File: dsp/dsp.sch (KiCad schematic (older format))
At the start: 29 parts

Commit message: Added ESP01 to DSPbox
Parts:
- added C? (x2): C, symbol C
- added U?: ESP01, symbol ESP01
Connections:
- net labels added: ESP_RX, ESP_TX
- wire segments 46 -> 51
- no-connect marks 13 -> 15
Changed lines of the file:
@@
 LIBS:valves
 LIBS:stm32f405rxtx
+LIBS:esp01
+LIBS:dsp-cache
 EELAYER 25 0
 EELAYER END
@@
 Text Label 7900 4600 0    60   ~ 0
 LCD_SCK
+$Comp
+L ESP01 U?
+U 1 1 574498BF
+P 5125 7250
+F 0 "U?" V 5175 7250 60  0000 C CNN
+F 1 "ESP01" V 5075 7250 60  0000 C CNN
+F 2 "" H 5125 7250 60  0000 C CNN
+F 3 "" H 5125 7250 60  0000 C CNN
+	1    5125 7250
+	1    0    0    -1
+$EndComp
+NoConn ~ 4525 7200
+NoConn ~ 4525 7300
+Wire Wire Line
+	5800 7300 5725 7300
+Wire Wire Line
+	5800 7000 5800 7300
+Wire Wire Line
+	5800 7200 5725 7200
+Wire Wire Line
+	5800 7100 5725 7100
+Connection ~ 5800 7200
+$Comp
+L +3V3 #PWR?
+U 1 1 57449FD5
+P 5800 7000
+F 0 "#PWR?" H 5800 6850 50  0001 C CNN
+F 1 "+3V3" H 5800 7140 50  0000 C CNN
+F 2 "" H 5800 7000 50  0000 C CNN
+F 3 "" H 5800 7000 50  0000 C CNN
+	1    5800 7000
+	1    0    0    -1
+$EndComp
+Connection ~ 5800 7100
+$Comp
+L C C?
+U 1 1 5744A312
+P 6375 7175
+F 0 "C?" H 6400 7275 50  0000 L CNN
+F 1 "C" H 6400 7075 50  0000 L CNN
+F 2 "" H 6413 7025 50  0000 C CNN
+F 3 "" H 6375 7175 50  0000 C CNN
+	1    6375 7175
+	1    0    0    -1
+$EndComp
+Wire Wire Line
+	5800 7025 6575 7025
+Connection ~ 5800 7025
+$Comp
+L C C?
+U 1 1 5744A47B
+P 6575 7175
+F 0 "C?" H 6600 7275 50  0000 L CNN
+F 1 "C" H 6600 7075 50  0000 L CNN
+F 2 "" H 6613 7025 50  0000 C CNN
+F 3 "" H 6575 7175 50  0000 C CNN
+	1    6575 7175
+	1    0    0    -1
+$EndComp
+Connection ~ 6375 7025
+$Comp
+L GND #PWR?
+U 1 1 5744A574
+P 6375 7325
+F 0 "#PWR?" H 6375 7075 50  0001 C CNN
+F 1 "GND" H 6375 7175 50  0000 C CNN
+F 2 "" H 6375 7325 50  0000 C CNN
+F 3 "" H 6375 7325 50  0000 C CNN
+	1    6375 7325
+	1    0    0    -1
+$EndComp
+$Comp
+L GND #PWR?
+U 1 1 5744A5C8
+P 6575 7325
+F 0 "#PWR?" H 6575 7075 50  0001 C CNN
+F 1 "GND" H 6575 7175 50  0000 C CNN
+F 2 "" H 6575 7325 50  0000 C CNN
+F 3 "" H 6575 7325 50  0000 C CNN
+	1    6575 7325
+	1    0    0    -1
+$EndComp
+Text Label 5725 7400 0    60   ~ 0
+ESP_TX
+Text Label 4525 7100 2    60   ~ 0
+ESP_RX
+$Comp
+L GND #PWR?
+U 1 1 5744B7D7
+P 4525 7400
+F 0 "#PWR?" H 4525 7150 50  0001 C CNN
+F 1 "GND" H 4525 7250 50  0000 C CNN
+F 2 "" H 4525 7400 50  0000 C CNN
+F 3 "" H 4525 7400 50  0000 C CNN
+	1    4525 7400
+	1    0    0    -1
+$EndComp
+Wire Notes Line
+	4175 6800 6750 6800
+Wire Notes Line
+	4175 6800 4175 7600
+Wire Notes Line
+	4175 7600 6750 7600
+Wire Notes Line
+	6750 7600 6750 6800
+Text Label 7900 4800 0    60   ~ 0
+ESP_RX
+Text Label 7900 4900 0    60   ~ 0
+ESP_TX
 $EndSCHEMATC

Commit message: Higher impedance inst inputs
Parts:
- removed C?: CP, symbol CP
- removed U? (x2): MCP601, symbol MCP601
- added C?: 100n, symbol C
- added U?: NE5532, symbol NE5532
- R?: value 1M -> 10M
- R?: value 100k -> 10M
- R?: value 10k -> 1M
- R?: value 100k -> 1M
- R? (x2): value 100R -> 100k
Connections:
- wire segments 51 -> 68
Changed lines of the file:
@@
 P 1900 1700
 F 0 "R?" H 1970 1746 50  0000 L CNN
-F 1 "1M" H 1970 1654 50  0000 L CNN
+F 1 "10M" H 1970 1654 50  0000 L CNN
 F 2 "" V 1830 1700 50  0000 C CNN
 F 3 "" H 1900 1700 50  0000 C CNN
@@
 $EndComp
 Wire Wire Line
-	1650 1550 2150 1550
+	1650 1550 1900 1550
+Wire Wire Line
+	1900 1550 2150 1550
 $Comp
 L GND #PWR?
@@
 P 2600 1350
 F 0 "R?" H 2670 1396 50  0000 L CNN
-F 1 "100k" H 2670 1304 50  0000 L CNN
+F 1 "10M" H 2670 1304 50  0000 L CNN
 F 2 "" V 2530 1350 50  0000 C CNN
 F 3 "" H 2600 1350 50  0000 C CNN
@@
 Wire Wire Line
 	2600 1550 2600 1500
-$Comp
-L MCP601 U?
-U 1 1 5743A901
-P 3600 1450
-F 0 "U?" H 3941 1496 50  0000 L CNN
-F 1 "MCP601" H 3941 1404 50  0000 L CNN
-F 2 "" H 3550 1550 50  0000 C CNN
-F 3 "" H 3650 1650 50  0000 C CNN
-	1    3600 1450
-	1    0    0    -1
-$EndComp
 Text Label 3300 1350 2    60   ~ 0
 VREF
@@
 P 3000 1550
 F 0 "R?" V 3208 1550 50  0000 C CNN
-F 1 "10k" V 3116 1550 50  0000 C CNN
+F 1 "1M" V 3116 1550 50  0000 C CNN
 F 2 "" V 2930 1550 50  0000 C CNN
 F 3 "" H 3000 1550 50  0000 C CNN
@@
 $EndComp
 Wire Wire Line
-	2450 1550 2850 1550
-Wire Wire Line
-	3150 1550 3300 1550
+	2450 1550 2600 1550
+Wire Wire Line
+	2600 1550 2850 1550
+Wire Wire Line
+	3150 1550 3200 1550
+Wire Wire Line
+	3200 1550 3300 1550
 $Comp
 L R R?
@@
 P 3700 2100
 F 0 "R?" V 3492 2100 50  0000 C CNN
-F 1 "100k" V 3584 2100 50  0000 C CNN
+F 1 "1M" V 3584 2100 50  0000 C CNN
 F 2 "" V 3630 2100 50  0000 C CNN
 F 3 "" H 3700 2100 50  0000 C CNN
@@
 P 1750 2650
 F 0 "R?" H 1820 2696 50  0000 L CNN
-F 1 "100R" H 1820 2604 50  0000 L CNN
+F 1 "100k" H 1820 2604 50  0000 L CNN
 F 2 "" V 1680 2650 50  0000 C CNN
 F 3 "" H 1750 2650 50  0000 C CNN
@@
 P 1750 3050
 F 0 "R?" H 1820 3096 50  0000 L CNN
-F 1 "100R" H 1820 3004 50  0000 L CNN
+F 1 "100k" H 1820 3004 50  0000 L CNN
 F 2 "" V 1680 3050 50  0000 C CNN
 F 3 "" H 1750 3050 50  0000 C CNN
@@
 $EndComp
 Wire Wire Line
-	1750 2800 1750 2900
-Wire Wire Line
-	1750 2850 2400 2850
+	1750 2800 1750 2850
+Wire Wire Line
+	1750 2850 1750 2900
+Wire Wire Line
+	1750 2850 2150 2850
+Wire Wire Line
+	2150 2850 2300 2850
 Connection ~ 1750 2850
-$Comp
-L MCP601 U?
-U 1 1 5743AE10
-P 2700 2950
-F 0 "U?" H 3041 2996 50  0000 L CNN
-F 1 "MCP601" H 3041 2904 50  0000 L CNN
-F 2 "" H 2650 3050 50  0000 C CNN
-F 3 "" H 2750 3150 50  0000 C CNN
-	1    2700 2950
-	1    0    0    -1
-$EndComp
-$Comp
-L GND #PWR?
-U 1 1 5743AE82
-P 2600 3250
-F 0 "#PWR?" H 2600 3000 50  0001 C CNN
-F 1 "GND" H 2608 3076 50  0001 C CNN
-F 2 "" H 2600 3250 50  0000 C CNN
-F 3 "" H 2600 3250 50  0000 C CNN
-	1    2600 3250
-	1    0    0    -1
-$EndComp
-$Comp
-L +9V #PWR?
-U 1 1 5743AEB7
-P 2600 2650
-F 0 "#PWR?" H 2600 2500 50  0001 C CNN
-F 1 "+9V" H 2618 2824 50  0000 C CNN
-F 2 "" H 2600 2650 50  0000 C CNN
-F 3 "" H 2600 2650 50  0000 C CNN
-	1    2600 2650
-	1    0    0    -1
-$EndComp
-Wire Wire Line
-	2400 3050 2400 3400
-Wire Wire Line
-	2400 3400 3000 3400
-Wire Wire Line
-	3000 3400 3000 2950
-Wire Wire Line
-	3000 2950 3150 2950
-Text Label 3150 2950 0    60   ~ 0
+Text Label 2300 2850 0    60   ~ 0
 VREF
-$Comp
-L CP C?
-U 1 1 5743AF79
-P 2150 3050
-F 0 "C?" H 2268 3096 50  0000 L CNN
-F 1 "CP" H 2268 3004 50  0000 L CNN
-F 2 "" H 2188 2900 50  0000 C CNN
-F 3 "" H 2150 3050 50  0000 C CNN
-	1    2150 3050
-	1    0    0    -1
-$EndComp
 Connection ~ 2150 2850
 $Comp
@@
 $EndComp
 Wire Wire Line
-	950  5100 1200 5100
+	950  5100 1050 5100
+Wire Wire Line
+	1050 5100 1200 5100
 Wire Wire Line
 	1050 5100 1050 5200
@@
 $EndComp
 Wire Wire Line
-	1800 5100 2000 5100
+	1800 5100 1900 5100
+Wire Wire Line
+	1900 5100 2000 5100
 Wire Wire Line
 	1900 5100 1900 5200
@@
 	6150 2100 5800 2100
 Wire Wire Line
-	5800 2000 5800 2400
+	5800 2000 5800 2100
+Wire Wire Line
+	5800 2100 5800 2200
+Wire Wire Line
+	5800 2200 5800 2300
+Wire Wire Line
+	5800 2300 5800 2400
 Wire Wire Line
 	5800 2200 6150 2200
@@
 	6150 2700 5800 2700
 Wire Wire Line
-	5800 2600 5800 2800
+	5800 2600 5800 2700
+Wire Wire Line
+	5800 2700 5800 2800
 Wire Wire Line
 	6150 2600 5800 2600
@@
 $EndComp
 Wire Wire Line
-	5500 3300 6150 3300
+	5500 3300 5550 3300
+Wire Wire Line
+	5550 3300 6150 3300
 Wire Wire Line
 	5550 3300 5550 3350
@@
 $EndComp
 Wire Wire Line
-	9650 2100 10050 2100
+	9650 2100 9750 2100
+Wire Wire Line
+	9750 2100 10050 2100
 Wire Wire Line
 	9750 2100 9750 2150
@@
 	2250 7300 2250 7550
 Wire Wire Line
-	2250 7550 3450 7550
+	2250 7550 3300 7550
+Wire Wire Line
+	3300 7550 3450 7550
 Wire Wire Line
 	2450 7300 2450 7400
 Wire Wire Line
-	2450 7400 3450 7400
+	2450 7400 2950 7400
+Wire Wire Line
+	2950 7400 3450 7400
 $Comp
 L R R?
@@
 $EndComp
 Wire Wire Line
-	10250 4050 10950 4050
+	10250 4050 10600 4050
+Wire Wire Line
+	10600 4050 10950 4050
 Wire Wire Line
 	10250 3950 10600 3950
 Wire Wire Line
-	10600 3750 10600 4050
+	10600 3750 10600 3950
+Wire Wire Line
+	10600 3950 10600 4050
 Connection ~ 10600 4050
 Wire Wire Line
@@
 	5800 7300 5725 7300
 Wire Wire Line
-	5800 7000 5800 7300
+	5800 7000 5800 7025
+Wire Wire Line
+	5800 7025 5800 7100
+Wire Wire Line
+	5800 7100 5800 7200
+Wire Wire Line
+	5800 7200 5800 7300
 Wire Wire Line
 	5800 7200 5725 7200
@@
 $EndComp
 Wire Wire Line
-	5800 7025 6575 7025
+	5800 7025 6375 7025
+Wire Wire Line
+	6375 7025 6575 7025
 Connection ~ 5800 7025
 $Comp
@@
 Text Label 7900 4900 0    60   ~ 0
 ESP_TX
+$Comp
+L C C?
+U 1 1 574593F7
+P 2150 3050
+F 0 "C?" H 2265 3096 50  0000 L CNN
+F 1 "100n" H 2265 3004 50  0000 L CNN
+F 2 "" H 2188 2900 50  0000 C CNN
+F 3 "" H 2150 3050 50  0000 C CNN
+	1    2150 3050
+	1    0    0    -1
+$EndComp
+$Comp
+L NE5532 U?
+U 1 1 57459598
+P 3600 1450
+F 0 "U?" H 3941 1496 50  0000 L CNN
+F 1 "NE5532" H 3941 1404 50  0000 L CNN
+F 2 "" H 3600 1450 50  0000 C CNN
+F 3 "" H 3600 1450 50  0000 C CNN
+	1    3600 1450
+	1    0    0    -1
+$EndComp
 $EndSCHEMATC

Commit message: DSP PCB
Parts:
- removed C? (x2): 10u, symbol CP
- removed C? (x2): C, symbol C
- removed J? (x2): JACK_2P, symbol JACK_2P
- removed R? (x2): 10M, symbol R
- removed R?: 1M, symbol R
- removed U?: AP1117D33, symbol AP1117D33
- removed U?: ESP01, symbol ESP01
- removed U?: NE5532, symbol NE5532
- added C10, C11, C7, C8, C9: 100n, agg:0603, symbol C_Small
- added C12, C13: 2u2, agg:0603, symbol C_Small
- added C14: C_Small, agg:0603, symbol C_Small
- added C15: C_Small, agg:1210, symbol C_Small
- added C16: 100n, agg:0603, symbol C
- added C5: 4u7, agg:0603, symbol C_Small
- added C6: 1u, agg:0603, symbol C_Small
- added D1: PMEG2005EH, dsp:SOD-123F, symbol D
- added P1: IN, Pin_Headers:Pin_Header_Straight_1x03, symbol CONN_01X03
- added P4: SWD_TC, agg:TC2030-NL, symbol SWD_TC
- added P5: OUT, Pin_Headers:Pin_Header_Straight_1x03, symbol CONN_01X03
- added P7: CONN_01X07, Pin_Headers:Pin_Header_Straight_1x07, symbol CONN_01X07
- added R5: 1k, agg:0603, symbol R
- added U1: NCP1117, TO_SOT_Packages_SMD:TO-252-2Lead, symbol NCP1117
- added U2: LM358N, agg:SOIC-8, symbol LM358N
- added U3: ESP02, dsp:esp02, symbol ESP02
- C1, C2: renamed from C?; value C -> 10u; footprint (none) -> agg:0603
- C3: renamed from C?; footprint (none) -> agg:0603
- C4: renamed from C?; value C -> 100n; footprint (none) -> agg:0603
- P2: renamed from P?; footprint (none) -> Pin_Headers:Pin_Header_Straight_1x02
- P3: renamed from P?; footprint (none) -> Pin_Headers:Pin_Header_Straight_1x03
- R1, R2, R3, R4, R6, R7: renamed from R?; footprint (none) -> agg:0603
- RV1, RV2, RV3, RV4: renamed from RV?; footprint (none) -> Pin_Headers:Pin_Header_Straight_1x03
- SW1: renamed from SW?; footprint (none) -> Pin_Headers:Pin_Header_Straight_1x02
- gave numbers to parts that had none: 2
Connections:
- net LCD_SCLK is gone; now on net LCD_SCK: P6.7 (P7)
- net LCD_SDA is gone; now on net LCD_MOSI: P6.8 (P8)
- net +3V3: now also IC1.1 (VBAT), C10.1, C11.1, C14.1, C15.1, C16.1, C5.1, C6.1, C7.1, C8.1, C9.1, D1.1 (K), P4.1 (VDD), P7.2 (P2), U1.2 (OUT), U3.4 (VCC)
- net ESP_RX: now also IC1.58 (PB6), U3.2 (RXD)
- net ESP_TX: now also IC1.59 (PB7), U3.3 (TXD)
- net FX_1: now also IC1.16 (PA2)
- net FX_2: now also IC1.21 (PA5)
- net FX_3: now also IC1.17 (PA3)
- net FX_SEL_A: now also IC1.14 (PA0)
- net FX_SEL_B: now also IC1.15 (PA1)
- net GND: now also P1.1 (P1), P5.1 (P1), U2.3 (+), U2.6 (-), U2.7; no longer C1.2, C2.2, C3.2, C4.2, IC1.12 (VSSA), IC1.18 (VSS), IC1.60 (BOOT0), IC1.63 (VSS), P2.1 (P1), P3.2 (P2), P6.1 (P1), P6.15 (P15), P6.17 (P17), P6.18 (P18), P6.20 (P20), R3.2, RV1.3, RV2.3, RV3.3
- net INST_IN: now also IC1.8 (PC0), D1.2 (A), R5.1; no longer R4.1
- net INST_OUT: now also IC1.20 (PA4)
- net LCD_RESET: now also IC1.37 (PC6), P7.7 (P7)
- net LCD_SCK: now also IC1.34 (PB13), P7.4 (P4)
- net at IC1.31 (VCAP_1): now also C12.1
- net LCD_CS: now reaches IC1.33 (PB12)
- net LCD_CS: now also P6.15 (P15), P7.6 (P6)
- net LCD_MOSI: now reaches IC1.36 (PB15)
- net LCD_MOSI: now also P7.5 (P5)
- net LCD_DC: now reaches IC1.38 (PC7)
- net LCD_DC: now also P6.4 (P4), P7.3 (P3)
- net SWDIO: now reaches IC1.46 (PA13)
- net SWDIO: now also P4.2 (SWDIO)
- net at IC1.47 (VCAP_2): now also C13.1
- net SWDCLK: now reaches IC1.49 (PA14)
- net SWDCLK: now also P4.4 (SWDCLK)
- net ESP_RST: now reaches IC1.57 (PB5)
- net ESP_RST: now also U3.8 (RST)
- net at R1.1: now also P1.2 (P2), P1.3 (P3)
- net at R1.2, R4.2: now also U2.2 (-)
- net at RV4.2: now also P5.2 (P2), P5.3 (P3)
- net +9V renamed VDD
- net VDD: now also U1.3 (IN), U2.8 (V+), U2.8 (V+)
- net NRST renamed nRST
- net nRST: now also P4.3 (~RST)
- net VREF: no longer names the net of C3.1, R2.2, R3.1
- net VREF: now also U2.5 (+)
- new net: R4.1, R5.2, U2.1
- new net VSS: C1.2, C10.2, C11.2, C12.2, C13.2, C14.2, C15.2, C16.2, C2.2, C3.2, C4.2, C5.2, C6.2, C7.2, C8.2, C9.2, IC1.12 (VSSA), IC1.18 (VSS), IC1.60 (BOOT0), IC1.63 (VSS), P2.1 (P1), P3.2 (P2), P4.5 (GND), P6.1 (P1), P6.17 (P17), P6.18 (P18), P6.20 (P20), P7.1 (P1), R3.2, RV1.3, RV2.3, RV3.3, U1.1 (GND), U2.4 (V-), U2.4 (V-), U3.1 (GND)
- no-connect marks 15 -> 14
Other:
- moved on the sheet: C4, IC1, P6, R1, R4, RV4

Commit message: Final tweaks
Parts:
- added C17, C18: 100n, agg:0603, symbol C
- added D2: LED, Pin_Headers:Pin_Header_Straight_1x02, symbol LED
- added R8: R, agg:0603, symbol R
- R2: value 100k -> 82k5
- R3: value 100k -> 18k7
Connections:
- net +3V3: now also R8.1
- net GND: now also C18.1
- net VDD: now also C17.1
- net VSS: now also C17.2, C18.2, D2.1 (K)
- new net: D2.2 (A), R8.2

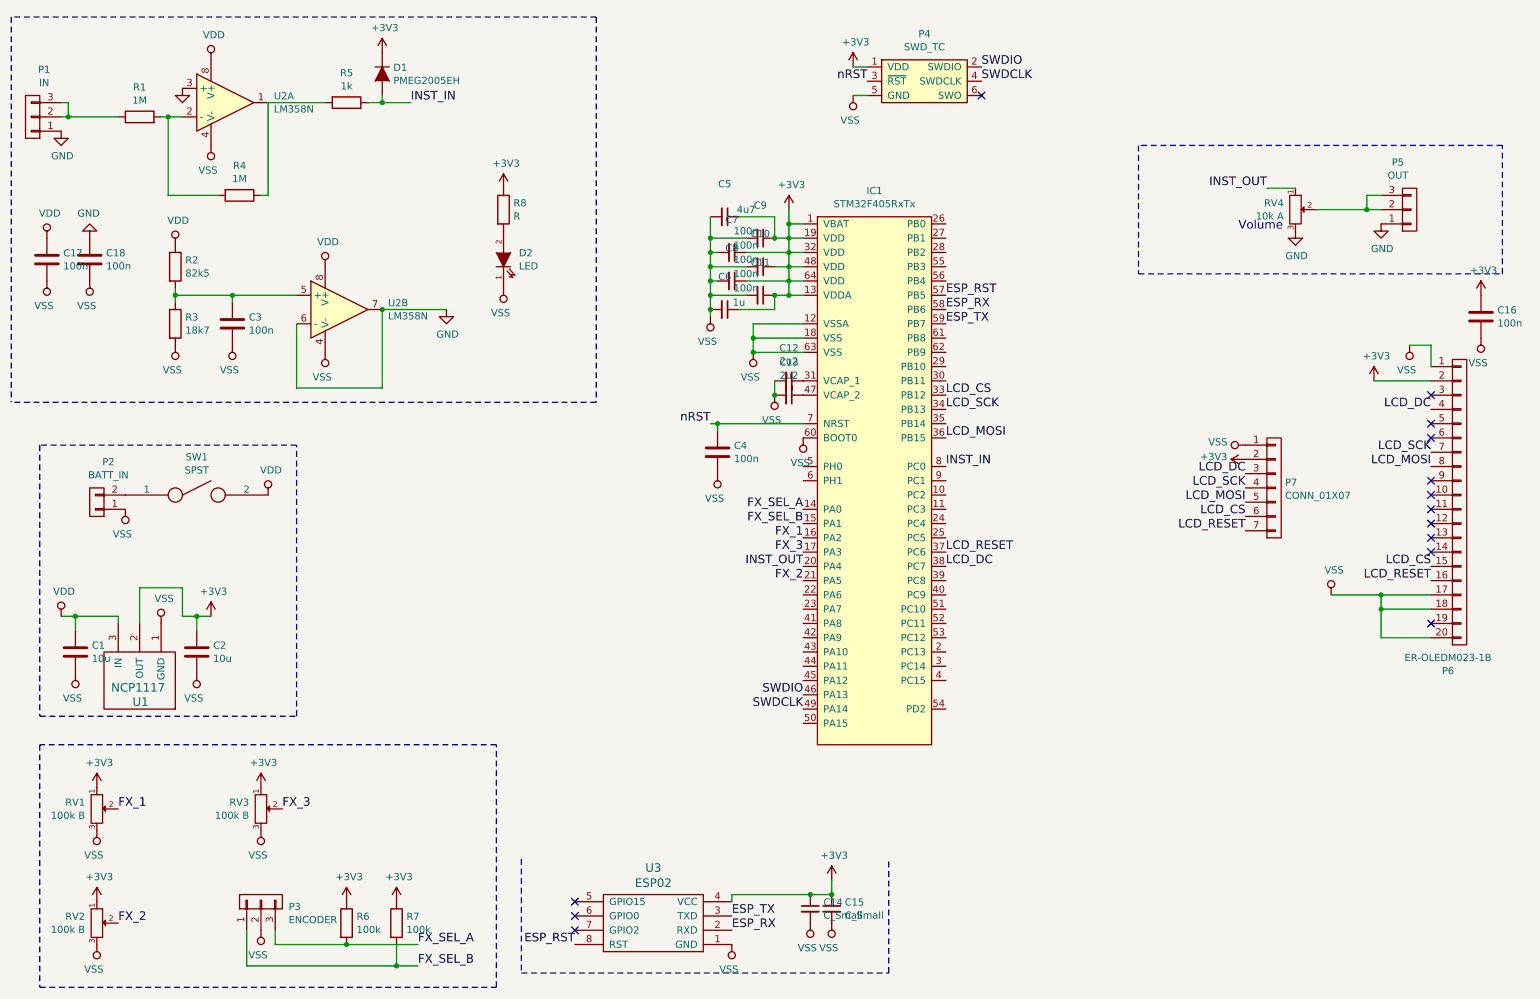
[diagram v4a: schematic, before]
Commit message: Added parts and bom for DSP
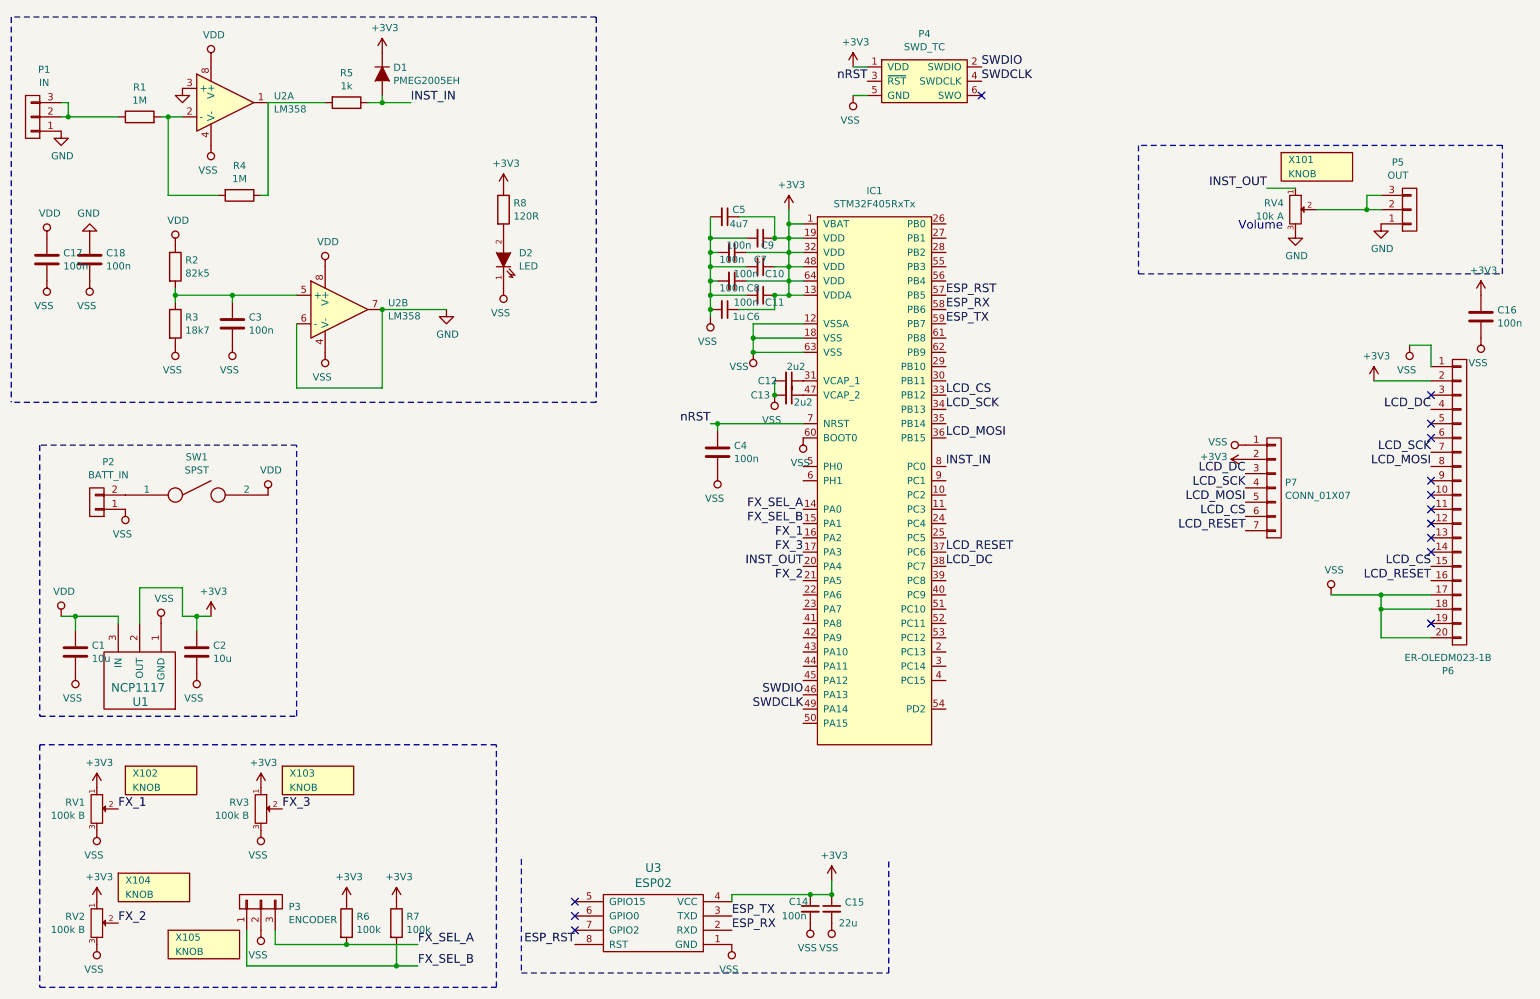
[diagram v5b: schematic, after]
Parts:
- added X101, X102, X103, X104, X105: KNOB, symbol PART
- C1, C2: Farnell (none) -> 2494233
- C10, C11, C16, C17, C18, C3, C4, C7, C8, C9: Farnell (none) -> 2524817
- C12, C13: Farnell (none) -> 2524865
- C14: value C_Small -> 100n; Farnell (none) -> 2524817
- C15: value C_Small -> 22u; Farnell (none) -> 2497179
- C5: Farnell (none) -> 2496930
- C6: Farnell (none) -> 2524858
- D1: Farnell (none) -> 1510671
- P1, P5: Farnell (none) -> 1217005
- P2: Farnell (none) -> BT06080
- P3: Farnell (none) -> 2065066
- R1, R4: Farnell (none) -> 9330410
- R2: Farnell (none) -> 1170978
- R3: Farnell (none) -> 1170914
- R5: Farnell (none) -> 9330380
- R6, R7: Farnell (none) -> 2309107
- R8: value R -> 120R; Farnell (none) -> 9330496
- RV1, RV2, RV3: Farnell (none) -> RE06791
- RV4: Farnell (none) -> 1760787
- U1: Farnell (none) -> 1652364
- U2: value LM358N -> LM358; Farnell (none) -> 2342291
